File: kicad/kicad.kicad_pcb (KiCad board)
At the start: 2 copper layers, 66 x 73 mm, 20 parts, among them IC1 IQRF_(DC)TR-72D, J1 Screw_Terminal_1x02, J2 Screw_Terminal_1x02, Q1 BSS138, Q2 BSS138, SW1 BondSW, U1 MeanWell_IRM-02

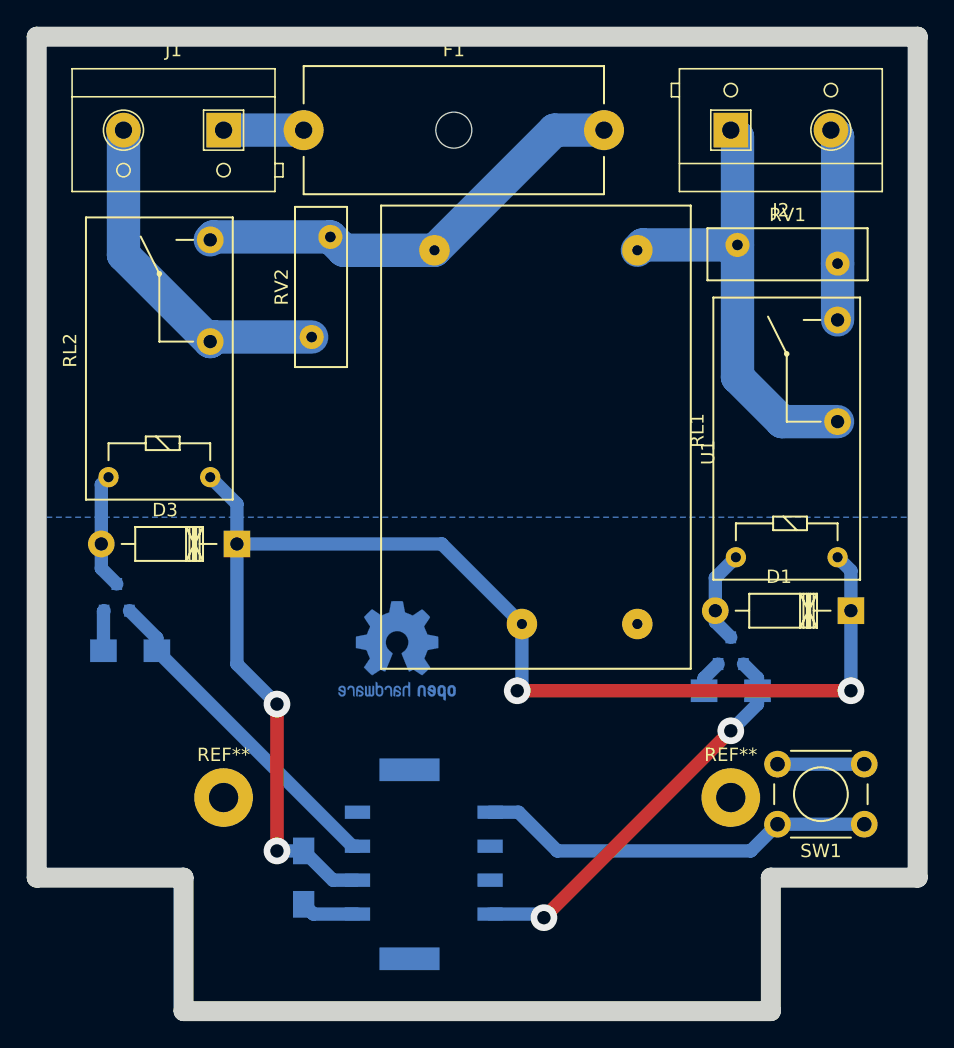
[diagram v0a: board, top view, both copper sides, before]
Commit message: Update schematic
Signed-off-by: Roman3349 <ondracek.roman@centrum.cz>
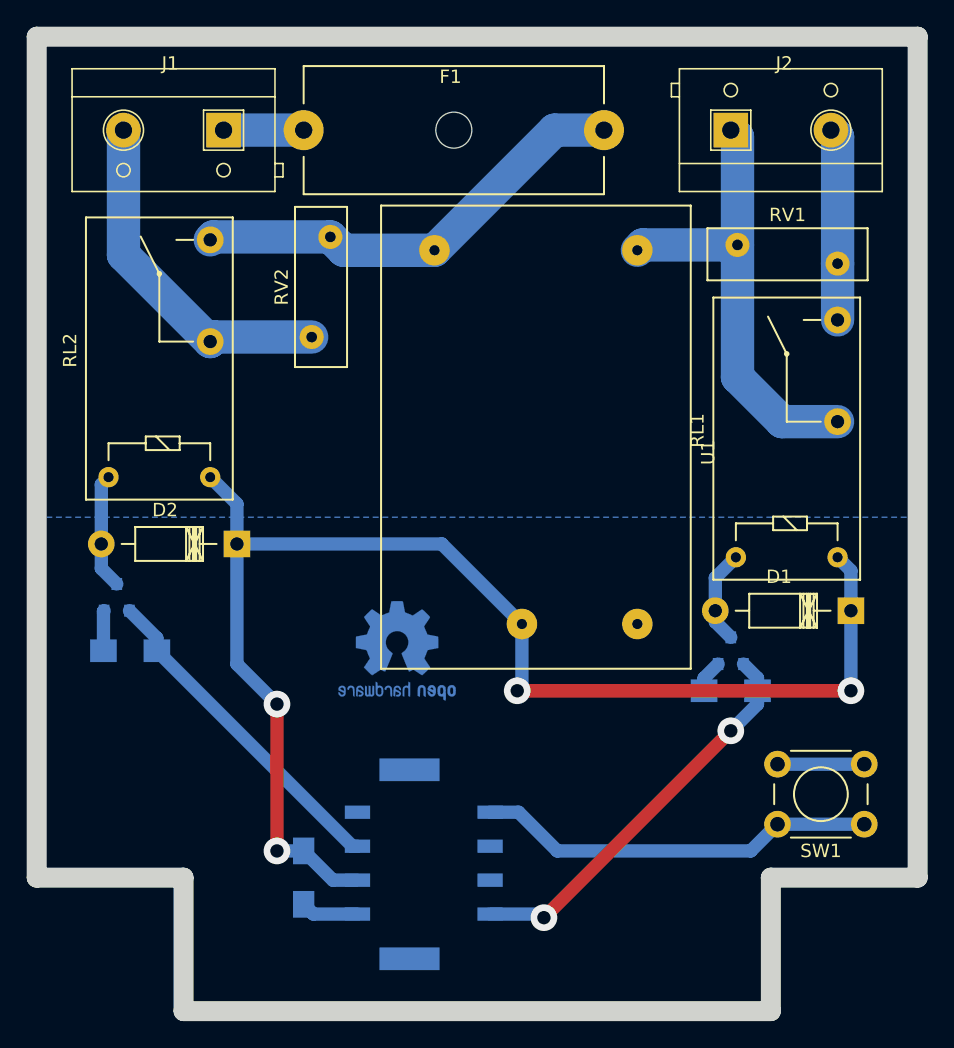
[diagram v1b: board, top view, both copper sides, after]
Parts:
- removed D3: 1N4007, Diodes_THT:Diode_DO-41_SOD81_Horizontal_RM10
- removed REF** (x2): MountingHole_2.2mm_M2_Pad, Mounting_Holes:MountingHole_2.2mm_M2_Pad
- added D2: 1N4007, Diodes_THT:Diode_DO-41_SOD81_Horizontal_RM10, F.Cu at (39.0, 74.0)
- IC1: value IQRF_(DC)TR-72D -> DCTR-72D
- U1: value MeanWell_IRM-02 -> IRM-02
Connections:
- net Lcurrent renamed Net-(IC1-Pad1)
